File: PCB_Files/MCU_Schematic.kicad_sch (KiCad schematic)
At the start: 36 parts, among them J10 2D_LiDAR, J2 Ultrasonic_Sensor, J3 OLED_Display, J5 USB_C_Receptacle_USB2.0_16P, J6 Conn_01x04_Pin, J9 IMU, SW1 SW_SPDT, U1 STM32F411RETx, Y1 16MHz

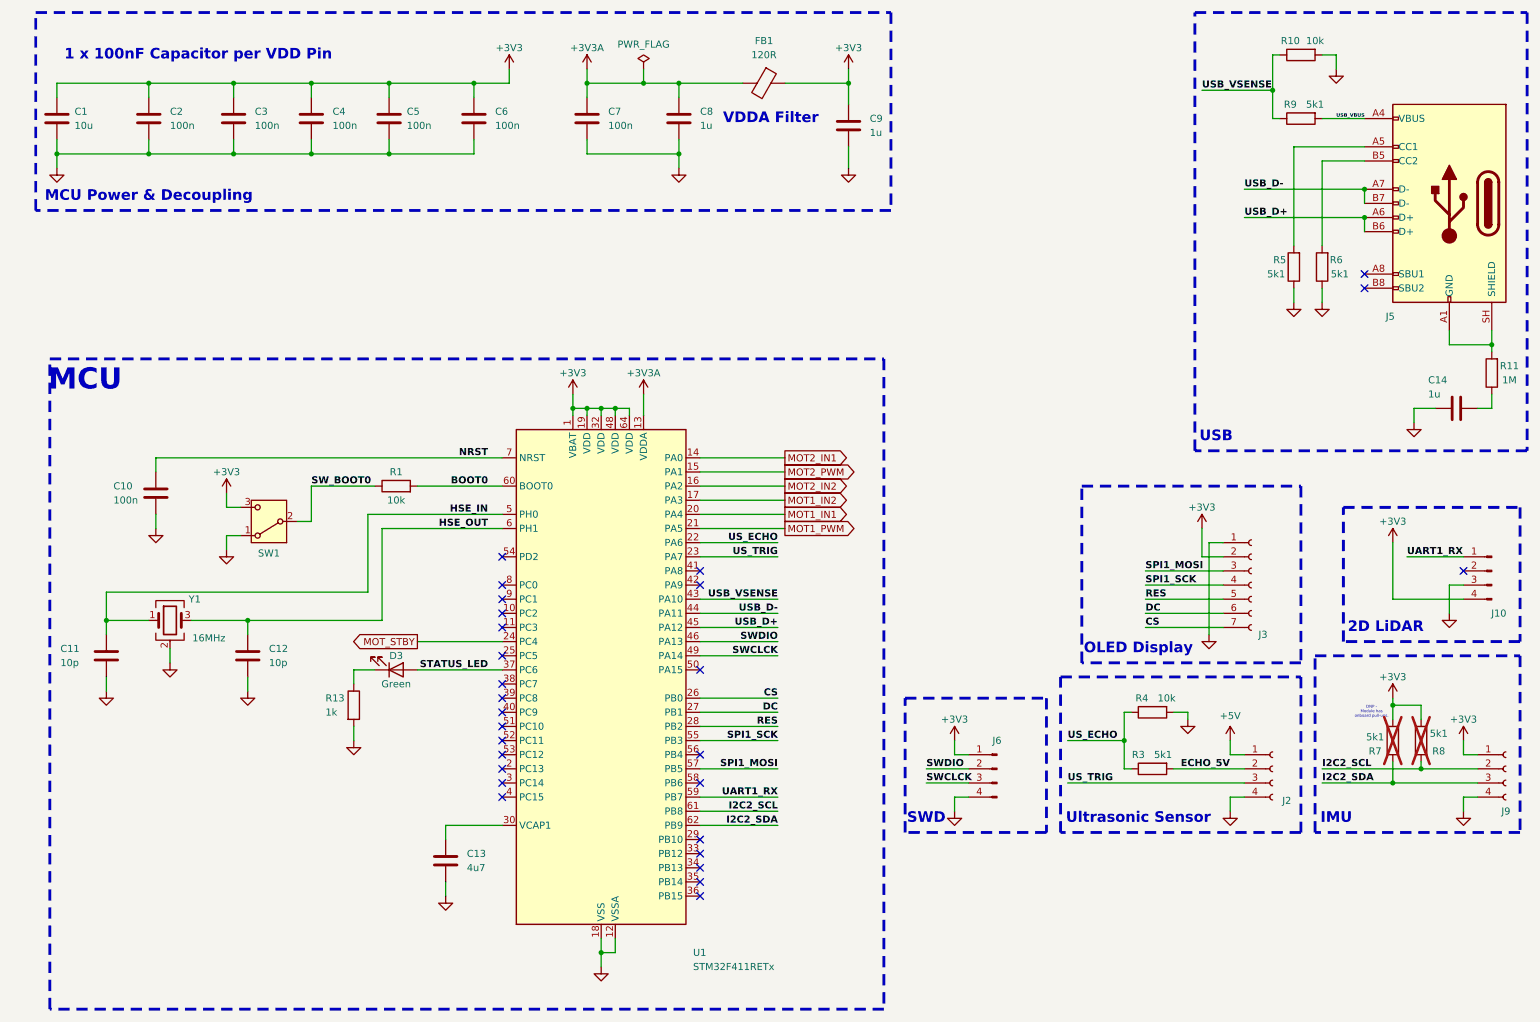
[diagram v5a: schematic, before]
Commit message: Added IC buck converter symbol and footprint to schematic. Will create own buck converter design on board.
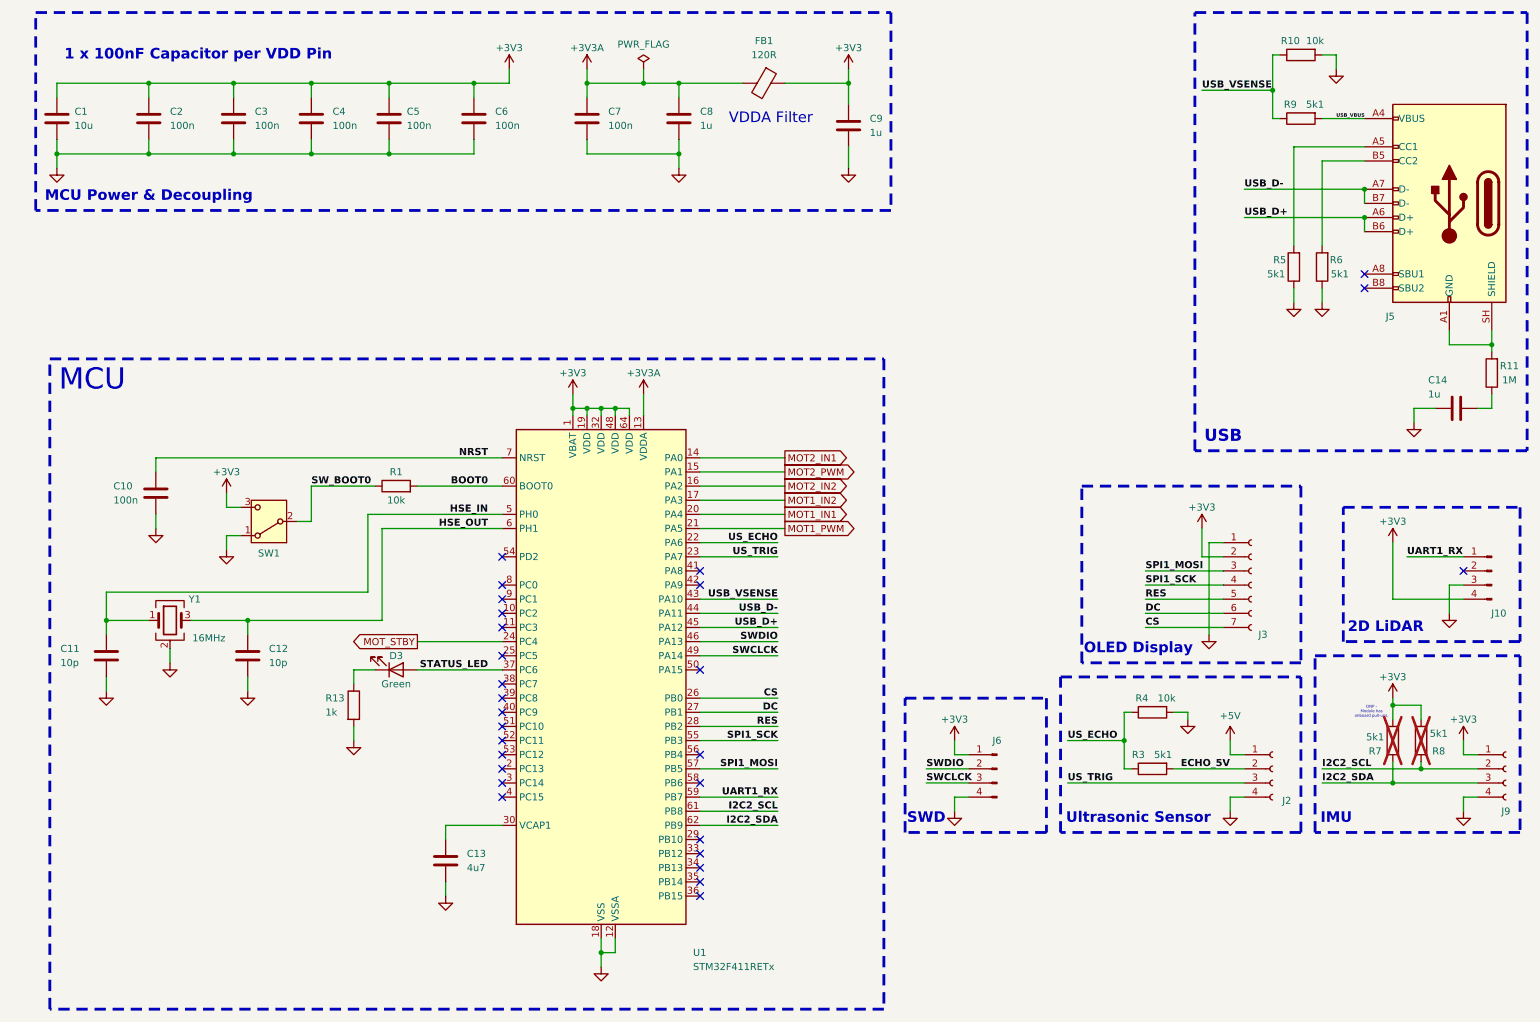
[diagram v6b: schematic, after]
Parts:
- C1, C13, C14, C8: footprint Capacitor_SMD:C_0603_1608Metric -> Capacitor_SMD:C_0805_2012Metric
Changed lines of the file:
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@@
 	(text "USB"
 		(exclude_from_sim no)
-		(at 227.33 90.17 0)
+		(at 228.6 90.17 0)
 		(effects
 			(font
-				(size 1.905 1.905)
-				(thickness 0.254)
+				(size 2.159 2.159)
+				(thickness 0.381)
 				(bold yes)
 				(color 0 0 255 1)
@@
 	(text "MCU"
 		(exclude_from_sim no)
-		(at 24.13 80.01 0)
+		(at 25.4 80.01 0)
 		(effects
 			(font
 				(size 3.81 3.81)
-				(thickness 0.254)
-				(bold yes)
+				(thickness 0.4763)
 				(color 0 0 255 1)
 			)
@@
 			(font
 				(size 0.508 0.508)
+				(thickness 0.0635)
 				(color 0 0 0 1)
 			)
@@
 			(font
 				(size 1.905 1.905)
-				(thickness 0.254)
+				(thickness 0.381)
 				(bold yes)
 				(color 0 0 255 1)
@@
 			(font
 				(size 1.905 1.905)
-				(thickness 0.254)
+				(thickness 0.381)
 				(bold yes)
 				(color 0 0 255 1)
@@
 			(font
 				(size 1.905 1.905)
-				(thickness 0.254)
+				(thickness 0.381)
 				(bold yes)
 				(color 0 0 255 1)
@@
 			(font
 				(size 1.905 1.905)
-				(thickness 0.254)
+				(thickness 0.381)
 				(bold yes)
 				(color 0 0 255 1)
@@
 			(font
 				(size 1.905 1.905)
-				(thickness 0.254)
+				(thickness 0.381)
 				(bold yes)
 				(color 0 0 255 1)
@@
 			(font
 				(size 1.905 1.905)
-				(thickness 0.254)
-				(bold yes)
+				(thickness 0.2381)
 				(color 0 0 255 1)
 			)
@@
 			(font
 				(size 1.905 1.905)
-				(thickness 0.254)
+				(thickness 0.381)
 				(bold yes)
 				(color 0 0 255 1)
@@
 			)
 		)
-		(property "Footprint" "Capacitor_SMD:C_0603_1608Metric"
+		(property "Footprint" "Capacitor_SMD:C_0805_2012Metric"
 			(at 20.0152 36.83 0)
 			(hide yes)
@@
 			)
 		)
-		(property "Footprint" "Capacitor_SMD:C_0603_1608Metric"
+		(property "Footprint" "Capacitor_SMD:C_0805_2012Metric"
 			(at 266.7 86.0552 0)
 			(hide yes)
@@
 			)
 		)
-		(property "Footprint" "Capacitor_SMD:C_0603_1608Metric"
+		(property "Footprint" "Capacitor_SMD:C_0805_2012Metric"
 			(at 87.9348 162.56 0)
 			(hide yes)
@@
 			)
 		)
-		(property "Footprint" "Capacitor_SMD:C_0603_1608Metric"
+		(property "Footprint" "Capacitor_SMD:C_0805_2012Metric"
 			(at 131.7752 36.83 0)
 			(hide yes)
